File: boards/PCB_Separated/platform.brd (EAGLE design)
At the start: 100.3 x 80 mm, 21 parts, among them IC1 FT232RL, U1 STM32F10XRXT6, X1 32khz, X8 8mhz

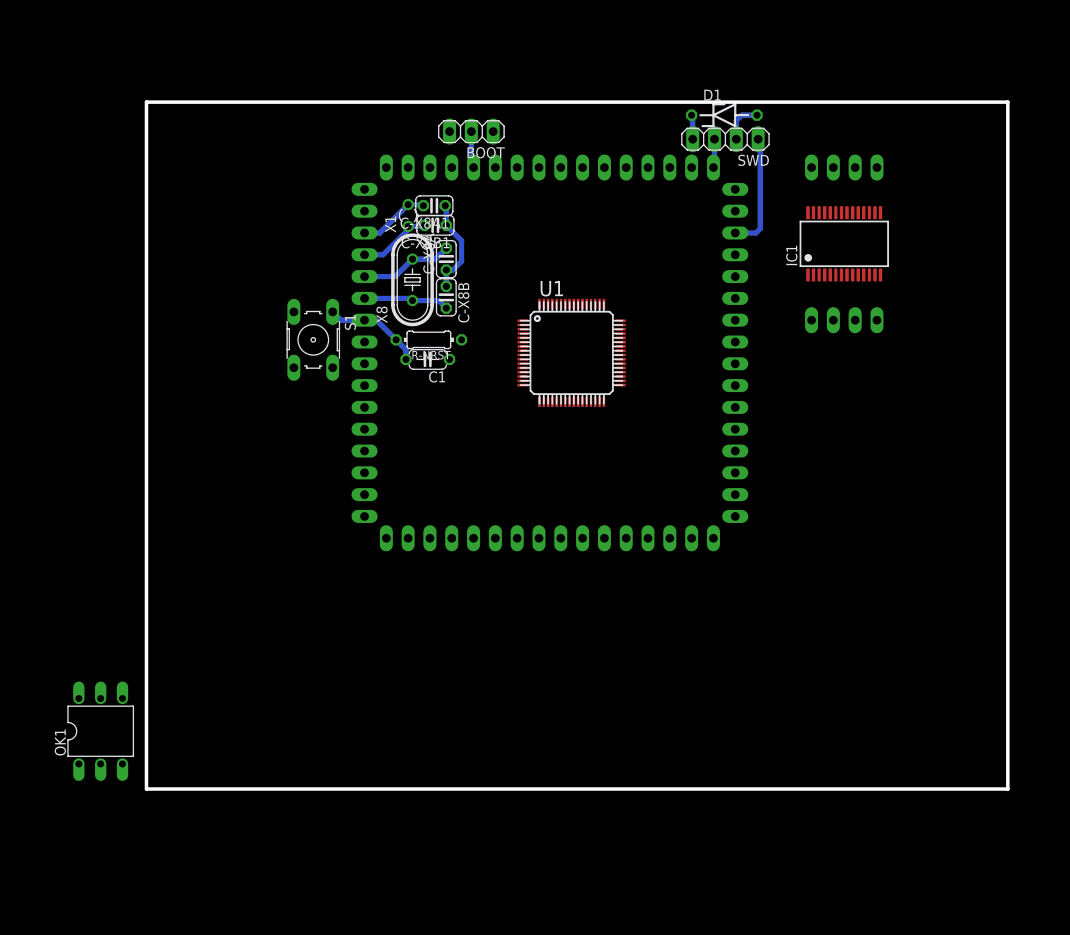
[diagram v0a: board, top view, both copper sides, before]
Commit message: -delete a useless sch pics -add ecu io pins diagram -add a GND to VSS line on FTDI. Hopefully internally connected with other GND pins -progress new separated ecu board.
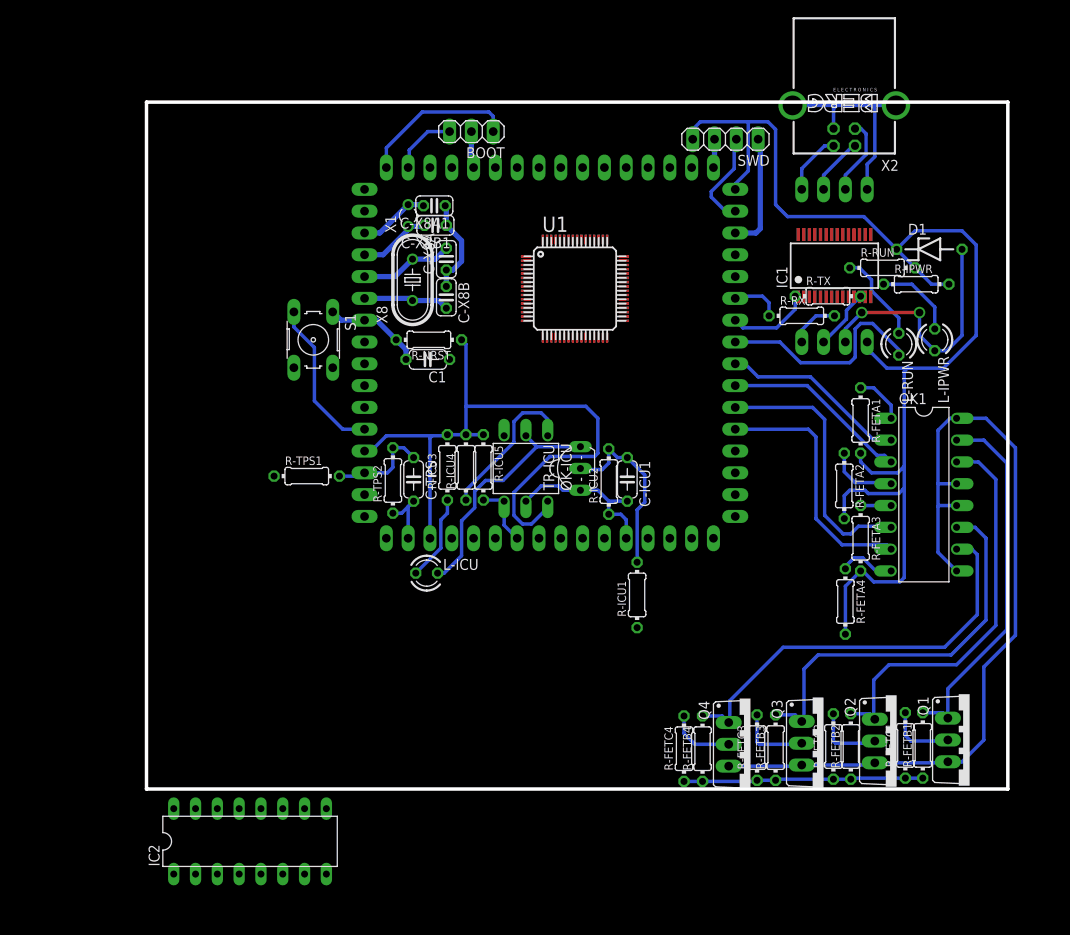
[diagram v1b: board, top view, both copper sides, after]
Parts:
- added C-ICU1, C-TPS: 100n, resistor:C050-024X044
- added IC2: L293D, st-microelectronics:DIL16
- added L-ICU, L-IPWR, L-RUN: (no value), led:LED3MM
- added OK-ICU: H11L1M, optocoupler:DIL06
- added Q1, Q2, Q3, Q4: IRF530, transistor-power:TO220BV
- added R-FETA1, R-FETA2, R-FETA3, R-FETA4, R-ICU3, R-ICU4, R-IPWR, R-RUN: 330, resistor:0204/7
- added R-FETB1, R-FETB2, R-FETB3, R-FETB4, R-FETC1, R-FETC2, R-FETC3, R-FETC4, R-ICU2, R-ICU5: 4k7, resistor:0204/7
- added R-ICU1, R-RX, R-TPS1, R-TPS2, R-TX: 1k, resistor:0204/7
- added TR-ICU: (no value), transistor-neu-to92:TO92-EBC
- added X2: PN61729-S, con-berg:PN61729-S
- OK1: value H11L1M -> ILQ1; device optocoupler:DIL06 -> optocoupler:DIL16
- moved OK1 99.8 mm to (90.6, 34.3), turned to 270 degrees
- moved D1 28.5 mm to (91.2, 62.9)
- moved U1 7.50 mm to (49.9, 58.3)
- moved IN 2.79 mm to (80.1, 69.8)
- moved IC1 2.79 mm to (80.1, 61.0)
- moved OUT 2.79 mm to (80.1, 52.1)
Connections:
- new net GND1: IC2.4
- new net GND2: IC2.5
- new net GND3: IC2.13
- new net GND4: IC2.12
- new net IGN1: Q3.D, R-FETC3.2
- new net IGN2: Q4.D, R-FETC4.2
- new net INJ1: Q1.D, R-FETC1.2
- new net INJ2: Q2.D, R-FETC2.2
- new net N$1: R-TPS1.1
- new net N$11: OK1.15, Q1.G, R-FETB1.2
- new net N$12: OK1.4, R-FETA2.1
- new net N$13: OK1.1, R-FETA1.1
- new net N$14: OK1.11, Q3.G, R-FETB3.2
- new net N$15: OK1.5, R-FETA3.1
- new net N$16: OK1.10, Q4.G, R-FETB4.2
- new net N$17: OK1.8, R-FETA4.1
- new net N$2: OK1.14, Q2.G, R-FETB2.2
- new net N$3: C-ICU1.1, R-ICU1.2, R-ICU2.2, TR-ICU.B
- new net N$4: L-ICU.K, OK-ICU.2, TR-ICU.C
- new net N$5: OK-ICU.1, R-ICU4.1
- new net N$6: L-ICU.A, R-ICU3.1
- new net N$7: L-IPWR.A, R-IPWR.1
- new net N$8: L-RUN.A, R-RUN.1
- new net N$9: R-ICU1.1
- new net V12: R-FETB1.1, R-FETB2.1, R-FETB3.1, R-FETB4.1, R-FETC1.1, R-FETC2.1, R-FETC3.1, R-FETC4.1
- new net VCC1: IC2.16
- new net VCC2: IC2.8
- net DM: now also X2.2
- net DP: now also X2.3
- net GND: now also OK1.12, OK1.13, OK1.16, OK1.9, Q1.S, Q2.S, Q3.S, Q4.S; no longer IC1.21, OK1.5
- net P14: now also C-TPS.1, R-TPS1.2, R-TPS2.2
- net P23: now also OK-ICU.4, R-ICU5.2
- net P37: now also OK1.7
- net P38: now also OK1.6
- net P39: now also OK1.3
- net P40: now also OK1.2
- net P41: now also L-RUN.K
- net P42: now also R-TX.1
- net P43: now also R-RX.1
- net RX: now also R-TX.2
- net TX: now also R-RX.2
- net VCC: now also X2.1; no longer OK1.6
- net VDD: now also OK-ICU.6, R-FETA1.2, R-FETA2.2, R-FETA3.2, R-FETA4.2, R-ICU3.2, R-ICU4.2, R-ICU5.1, R-IPWR.2, R-RUN.2
- net VSS: now also C-ICU1.2, C-TPS.2, IC1.21, L-IPWR.K, OK-ICU.5, R-ICU2.1, R-TPS2.1, TR-ICU.E, X2.4, X2.S1, X2.S2
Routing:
- net VDD: track 2.85 -> 242.8 mm
- net VSS: track 16.2 -> 131.1 mm, vias 0 -> 4
- net GND: track 0.00 -> 99.2 mm
- net N$16: track 0.00 -> 48.6 mm
- net N$2: track 0.00 -> 47.0 mm
- net N$14: track 0.00 -> 46.6 mm
- net N$11: track 0.00 -> 42.7 mm
- net P38: track 0.00 -> 31.2 mm
- net P37: track 0.00 -> 29.5 mm
- net N$4: track 0.00 -> 28.0 mm
- net V12: track 0.00 -> 28.0 mm
- net P41: track 0.00 -> 25.8 mm
- net P40: track 0.00 -> 21.8 mm
- net P39: track 0.00 -> 21.8 mm
- net N$3: track 0.00 -> 21.3 mm
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
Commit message: progress to build new ecu boards
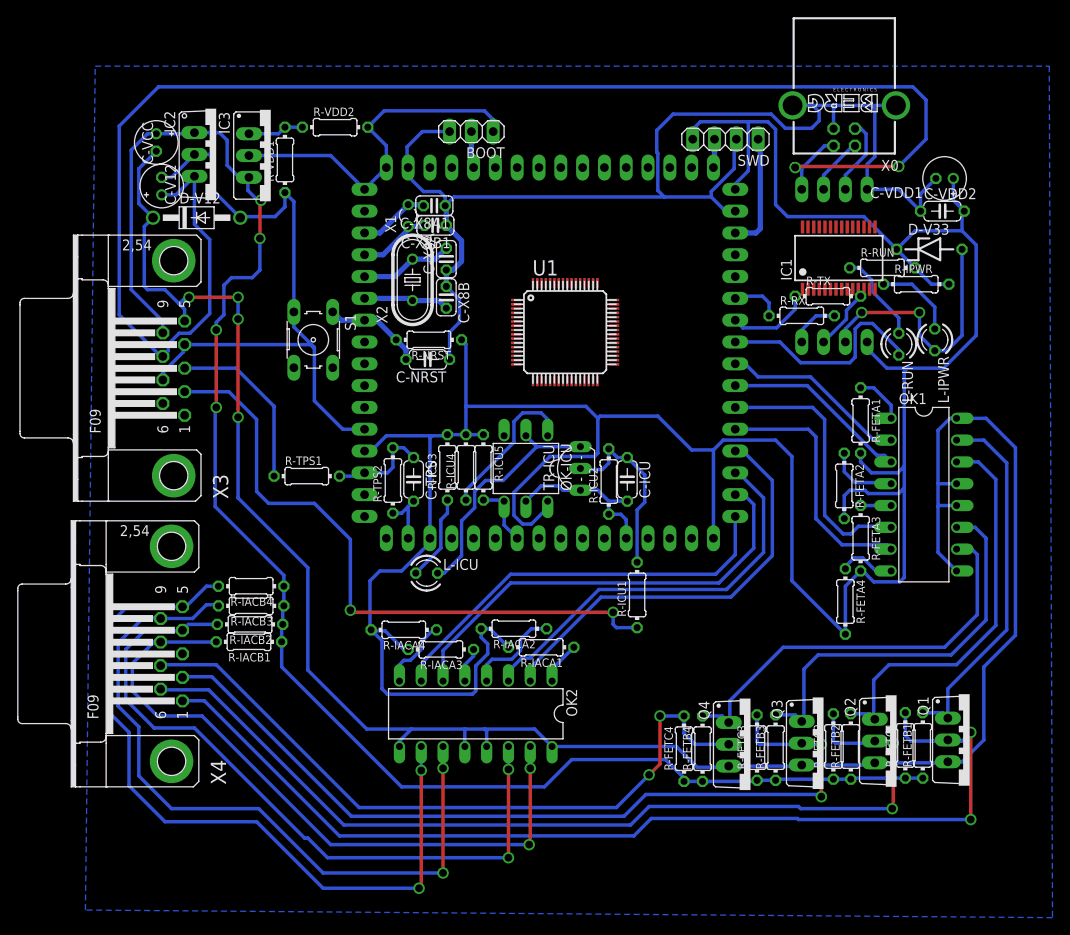
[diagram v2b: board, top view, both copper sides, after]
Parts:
- removed X8: 8mhz, crystal:HC49U-V
- added C-V12, C-VCC, C-VDD1: 100n/25v, resistor:E2-5
- added C-VDD2: 100n, resistor:C050-024X044
- added D-V12: 1N4004, diode:DO41-10
- added IC3: (no value), v-reg:317TS
- added OK2: ILQ1, optocoupler:DIL16
- added R-IACA1, R-IACA2, R-IACA3, R-IACA4, R-VDD1: 330, resistor:0204/7
- added R-IACB1, R-IACB2, R-IACB3, R-IACB4: 4k7, resistor:0204/7
- added R-VDD2: 270, resistor:0204/7
- added X0: PN61729-S, con-berg:PN61729-S
- added X3, X4: (no value), con-subd:F09HP
- C-NRST: value (none) -> 100n
- IC2: value L293D -> 7805TV; device st-microelectronics:DIL16 -> linear:TO220V
- X2: value PN61729-S -> 8mhz; device con-berg:PN61729-S -> crystal:HC49U-V
- moved IC2 80.1 mm to (8.13, 73.9), turned to 270 degrees
- moved X2 54.2 mm to (31.0, 59.3), turned to 90 degrees
- moved U1 5.21 mm to (48.8, 53.2)
- moved IC1 1.02 mm to (80.6, 61.8)
- renumbered C-ICU1 to C-ICU, C1 to C-NRST, D1 to D-V33
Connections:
- removed net GND1: IC2.4
- removed net GND2: IC2.5
- removed net GND3: IC2.13
- removed net GND4: IC2.12
- removed net N$1: R-TPS1.1
- removed net N$9: R-ICU1.1
- removed net VCC1: IC2.16
- removed net VCC2: IC2.8
- new net IACA: OK2.15, R-IACB1.2, X4.8
- new net IACB: OK2.14, R-IACB2.2, X4.4
- new net IACC: OK2.11, R-IACB3.2, X4.9
- new net IACD: OK2.10, R-IACB4.2, X4.5
- new net ICU: R-ICU1.1, X3.2
- new net N$10: OK2.1, R-IACA1.1
- new net N$18: OK2.4, R-IACA2.1
- new net N$21: OK2.5, R-IACA3.1
- new net N$22: OK2.8, R-IACA4.1
- new net N$25: IC3.1, R-VDD1.2, R-VDD2.1
- new net TPS: R-TPS1.1, X3.3
- net DM: now also X0.2; no longer X2.2
- net DP: now also X0.3; no longer X2.3
- net GND: now also C-V12.-, D-V12.C, OK2.12, OK2.13, OK2.16, OK2.9, X3.5
- net IGN1: now also X4.2
- net IGN2: now also X4.7
- net INJ1: now also X4.1
- net INJ2: now also X4.6
- net P33: now also OK2.7
- net P34: now also OK2.6
- net P35: now also OK2.3
- net P36: now also OK2.2
- net P5: now also X2.2; no longer X8.2
- net P6: now also X2.1; no longer X8.1
- net V12: now also C-V12.+, IC2.1, IC3.3, R-IACB1.1, R-IACB2.1, R-IACB3.1, R-IACB4.1, X3.9
- net VCC: now also C-VCC.+, IC2.3, X0.1, X3.8; no longer X2.1
- net VDD: now also C-VDD1.+, C-VDD2.2, IC3.2, R-IACA1.2, R-IACA2.2, R-IACA3.2, R-IACA4.2, R-VDD2.2
- net VSS: now also C-VCC.-, C-VDD1.-, C-VDD2.1, D-V12.A, IC2.2, R-VDD1.1, X0.4, X0.S1, X0.S2, X3.4, X3.7; no longer X2.4, X2.S1, X2.S2
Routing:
- net VCC: track 7.22 -> 184.6 mm, vias 0 -> 3
- net V12: track 28.0 -> 189.4 mm, vias 0 -> 4
- net VSS: track 131.1 -> 282.8 mm
- net VDD: track 242.8 -> 383.0 mm
- net GND: track 99.2 -> 238.6 mm, vias 0 -> 4
- net INJ1: track 7.94 -> 120.6 mm, vias 0 -> 2
- net INJ2: track 8.21 -> 111.1 mm, vias 0 -> 2
- net IGN1: track 8.54 -> 99.4 mm, vias 0 -> 2
- net IACD: track 0.00 -> 89.5 mm, vias 0 -> 2
- net IACC: track 0.00 -> 85.0 mm, vias 0 -> 2
- net IACB: track 0.00 -> 82.9 mm, vias 0 -> 2
- net IACA: track 0.00 -> 79.2 mm, vias 0 -> 2
- net IGN2: track 7.77 -> 83.4 mm, vias 0 -> 2
- net ICU: track 0.00 -> 74.7 mm, vias 0 -> 2
- net P34: track 0.00 -> 52.4 mm
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- added copper zone on layer 16, net N$1
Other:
- board outline removed

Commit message: add connector board
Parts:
- C-V12, C-VCC, C-VDD1: value 100n/25v -> 100u/25v
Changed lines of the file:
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@@
 <layer number="18" name="Vias" color="2" fill="1" visible="yes" active="yes"/>
 <layer number="19" name="Unrouted" color="6" fill="1" visible="no" active="yes"/>
-<layer number="20" name="Dimension" color="15" fill="1" visible="yes" active="yes"/>
+<layer number="20" name="Dimension" color="15" fill="1" visible="no" active="yes"/>
 <layer number="21" name="tPlace" color="7" fill="1" visible="yes" active="yes"/>
-<layer number="22" name="bPlace" color="7" fill="1" visible="yes" active="yes"/>
+<layer number="22" name="bPlace" color="7" fill="1" visible="no" active="yes"/>
 <layer number="23" name="tOrigins" color="15" fill="1" visible="yes" active="yes"/>
-<layer number="24" name="bOrigins" color="15" fill="1" visible="yes" active="yes"/>
-<layer number="25" name="tNames" color="7" fill="1" visible="yes" active="yes"/>
-<layer number="26" name="bNames" color="7" fill="1" visible="yes" active="yes"/>
-<layer number="27" name="tValues" color="7" fill="1" visible="no" active="yes"/>
+<layer number="24" name="bOrigins" color="15" fill="1" visible="no" active="yes"/>
+<layer number="25" name="tNames" color="7" fill="1" visible="no" active="yes"/>
+<layer number="26" name="bNames" color="7" fill="1" visible="no" active="yes"/>
+<layer number="27" name="tValues" color="7" fill="1" visible="yes" active="yes"/>
 <layer number="28" name="bValues" color="7" fill="1" visible="no" active="yes"/>
 <layer number="29" name="tStop" color="7" fill="3" visible="no" active="yes"/>
@@
 <layer number="49" name="Reference" color="7" fill="1" visible="no" active="yes"/>
 <layer number="50" name="dxf" color="7" fill="1" visible="no" active="no"/>
-<layer number="51" name="tDocu" color="7" fill="1" visible="yes" active="yes"/>
-<layer number="52" name="bDocu" color="7" fill="1" visible="yes" active="yes"/>
+<layer number="51" name="tDocu" color="7" fill="1" visible="no" active="yes"/>
+<layer number="52" name="bDocu" color="7" fill="1" visible="no" active="yes"/>
 <layer number="91" name="Nets" color="2" fill="1" visible="no" active="no"/>
 <layer number="92" name="Busses" color="1" fill="1" visible="no" active="no"/>
@@
 <element name="R-VDD1" library="resistor" package="0204/7" value="330" x="16.129" y="73.279" rot="R90"/>
 <element name="R-VDD2" library="resistor" package="0204/7" value="270" x="21.971" y="77.089"/>
-<element name="C-V12" library="resistor" package="E2-5" value="100n/25v" x="1.143" y="75.311" rot="R270"/>
+<element name="C-V12" library="resistor" package="E2-5" value="100u/25v" x="1.143" y="75.311" rot="R270"/>
 <element name="D-V12" library="diode" package="DO41-10" value="1N4004" x="5.842" y="66.548"/>
-<element name="C-VCC" library="resistor" package="E2-5" value="100n/25v" x="1.778" y="70.231" rot="R90"/>
-<element name="C-VDD1" library="resistor" package="E2-5" value="100n/25v" x="92.964" y="71.12" rot="R180"/>
+<element name="C-VCC" library="resistor" package="E2-5" value="100u/25v" x="1.778" y="70.231" rot="R90"/>
+<element name="C-VDD1" library="resistor" package="E2-5" value="100u/25v" x="92.964" y="71.12" rot="R180"/>
 <element name="C-VDD2" library="resistor" package="C050-024X044" value="100n" x="92.71" y="67.31"/>
 <element name="X3" library="con-subd" package="F09HP" value="" x="3.175" y="49.022" rot="R90">
